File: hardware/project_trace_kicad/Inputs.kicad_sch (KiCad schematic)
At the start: 11 parts, among them J101 Conn_Coaxial, J102 Conn_Coaxial, U101 AD8421, U102 AQW280SX, U103 AQW280SX, U201 ADA4807-1

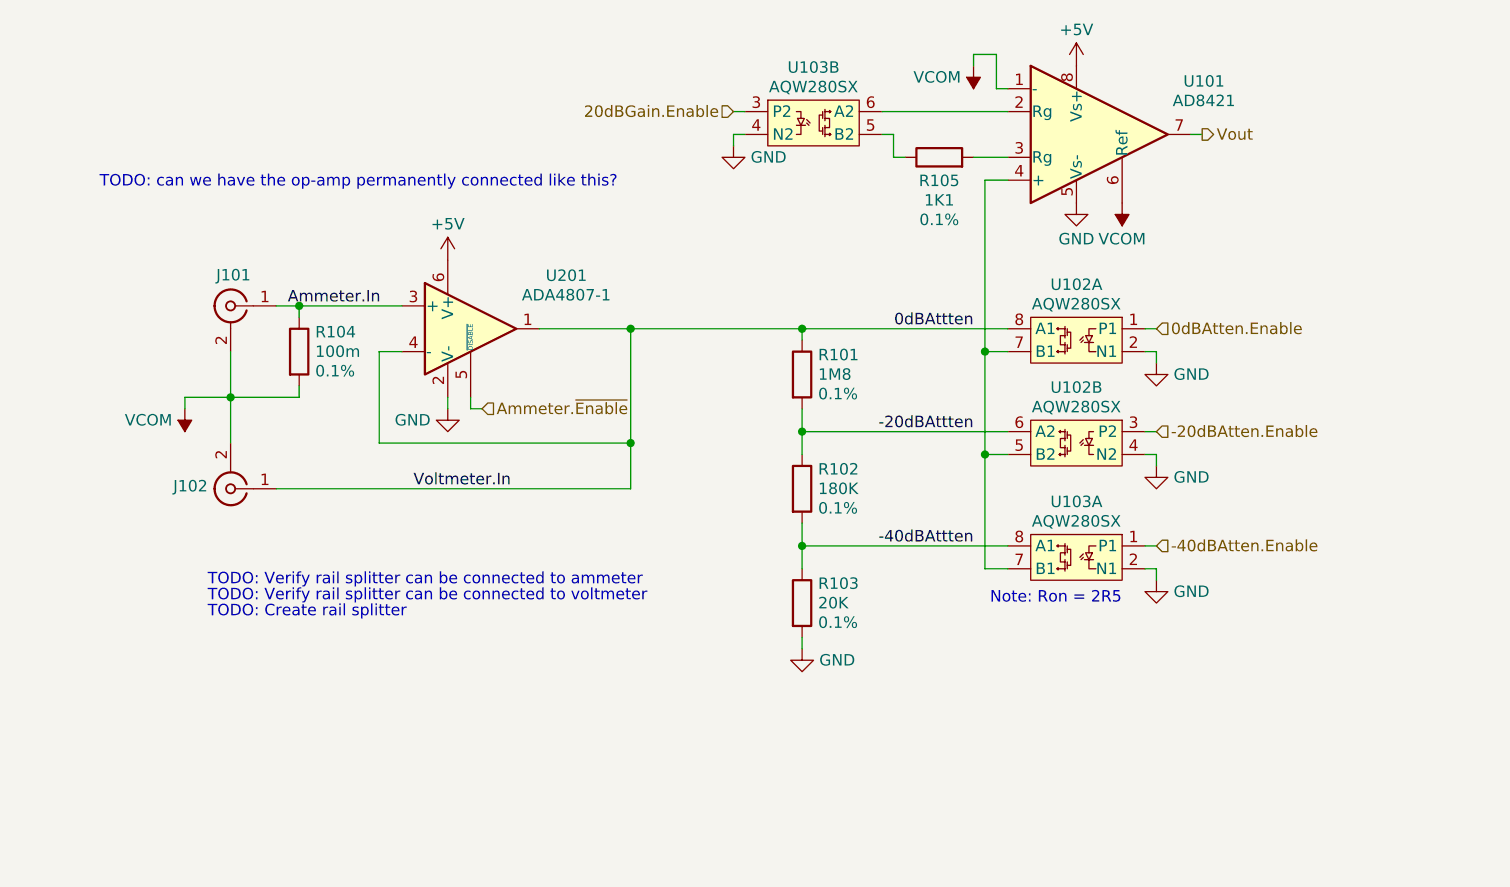
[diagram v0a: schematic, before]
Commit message: Add TVS, Fixes to Ammeter
Fix Ammeter OV Vulnerability
Choose Ammeter Current-Sensing Resistor
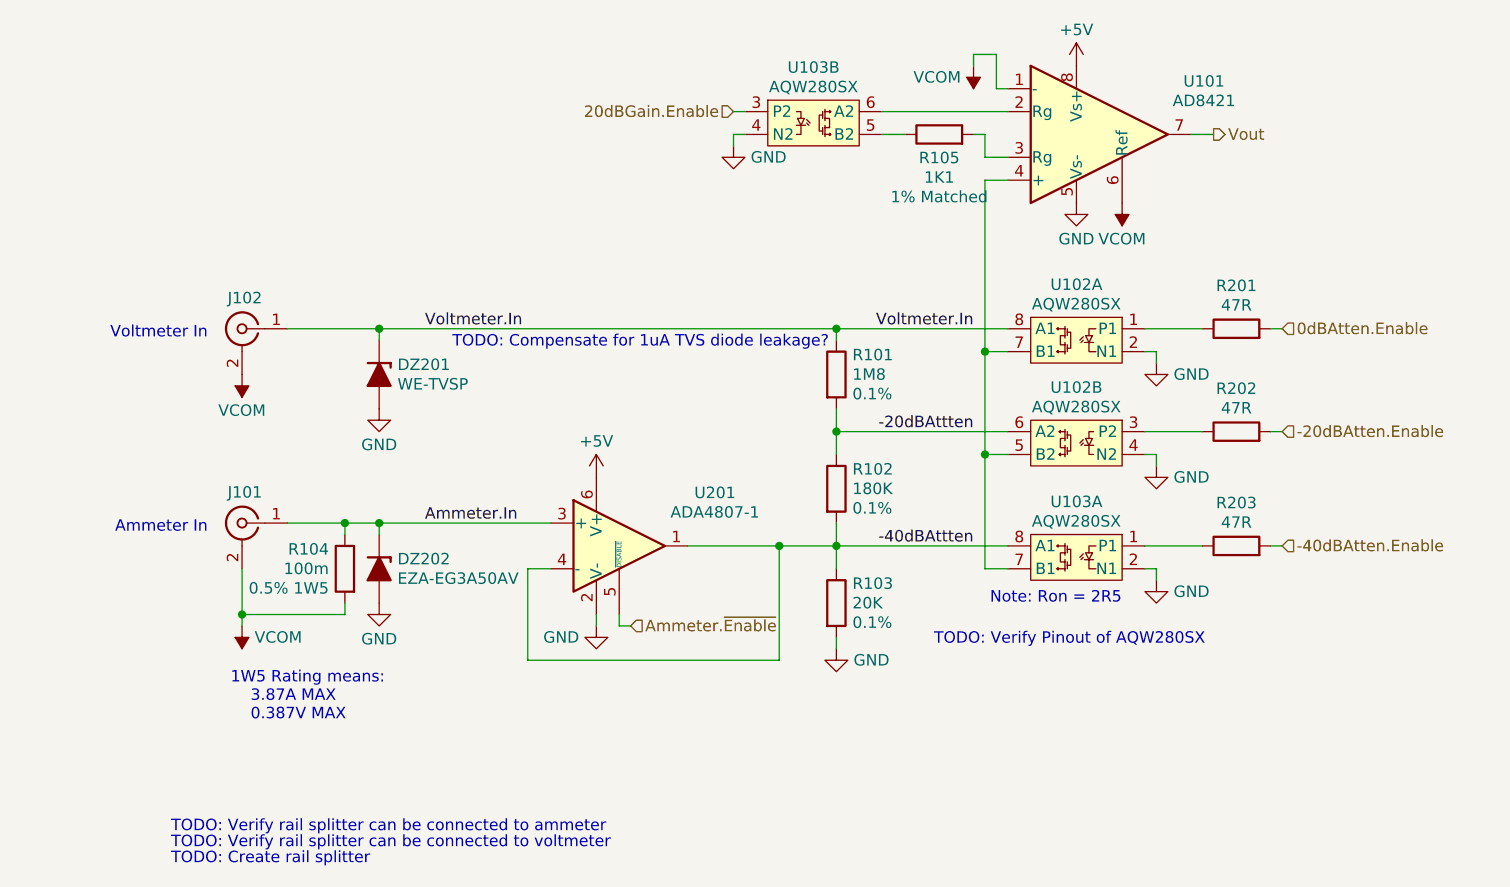
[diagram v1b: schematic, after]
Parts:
- added DZ201: WE-TVSP, Diode_SMD:D_SMC_Handsoldering, symbol PCM_Diode_Zener_AKL:D_Zener_Generic
- added DZ202: EZA-EG3A50AV, Diode_SMD:D_0603_1608Metric_Pad1.05x0.95mm_HandSolder, symbol PCM_Diode_Zener_AKL:D_Zener_Generic
- added R201, R202, R203: 47R, Resistor_SMD:R_0603_1608Metric_Pad0.98x0.95mm_HandSolder, symbol Device:R
- R104: footprint Resistor_SMD:R_0603_1608Metric_Pad0.98x0.95mm_HandSolder -> Resistor_SMD:R_2512_6332Metric_Pad1.40x3.35mm_HandSolder; Extra 0.1% -> 0.5% 1W5; MouserPN (none) -> SLW1TTER100D
- R105: Extra 0.1% -> 1% Matched
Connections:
- net -20dBAtten.Enable: now also R202.2; no longer U102.3 (P2)
- net -40dBAtten.Enable: now also R203.2; no longer U103.1 (P1)
- net -40dBAttten: now also U201.1, U201.4 (-)
- net 0dBAtten.Enable: now also R201.2; no longer U102.1 (P1)
- net Ammeter.In: now also DZ202.1 (K)
- net GND: now also DZ201.2 (A), DZ202.2 (A)
- net 0dBAttten renamed Voltmeter.In
- net Voltmeter.In: now also DZ201.1 (K); no longer U201.1, U201.4 (-)
- new net: R203.1, U103.1 (P1)
- new net: R201.1, U102.1 (P1)
- new net: R202.1, U102.3 (P2)
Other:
- note added: "1W5 Rating means: 3.87A MAX 0.387V MAX"
- note added: "Ammeter In"
- note added: "TODO: Compensate for 1uA TVS diode leakage?"
- note added: "TODO: Verify Pinout of AQW280SX"
- note added: "Voltmeter In"
- note removed: "TODO: can we have the op-amp permanently connected like this?"
- moved on the sheet: J101, J102, R101, R102, R103, R104, R105, U201

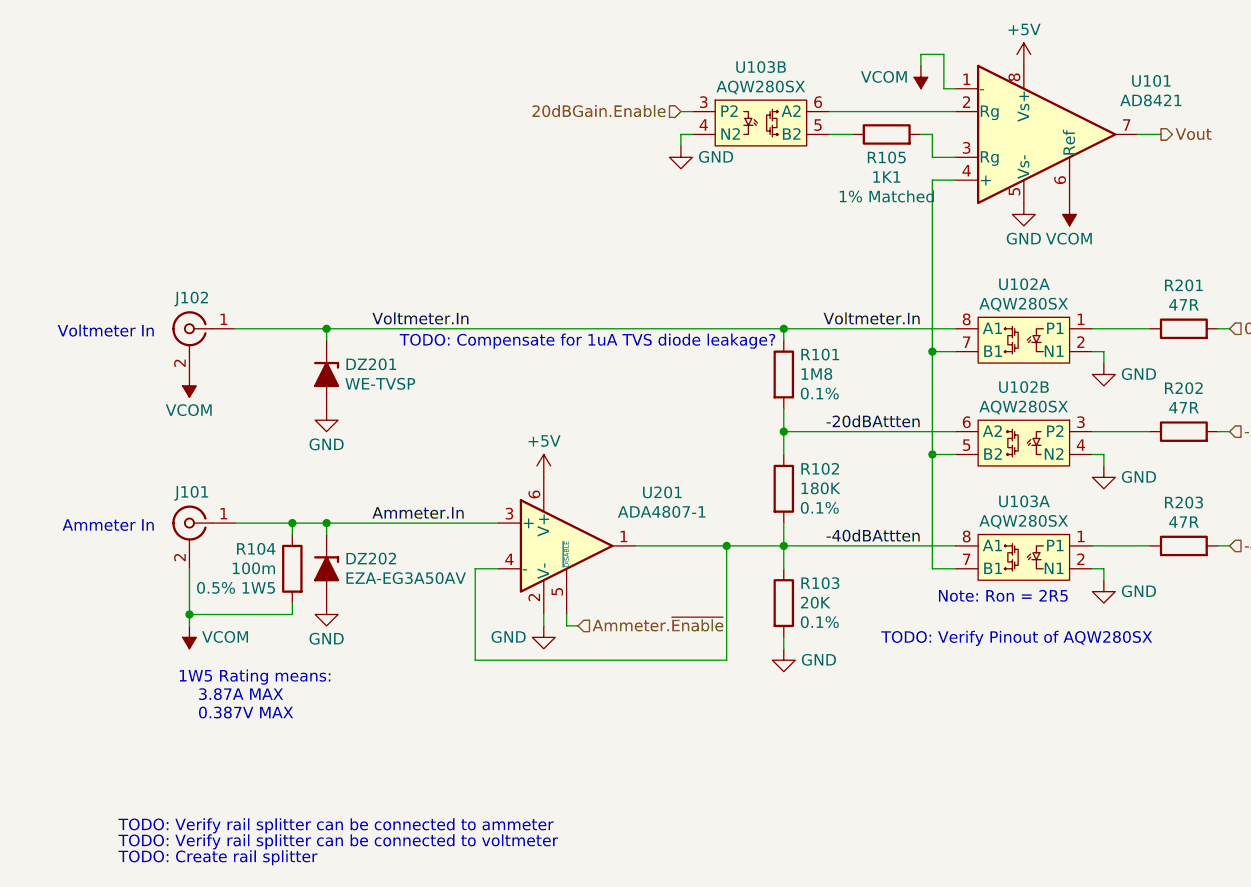
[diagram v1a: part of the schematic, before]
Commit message: Add TVS Diode to VCOM
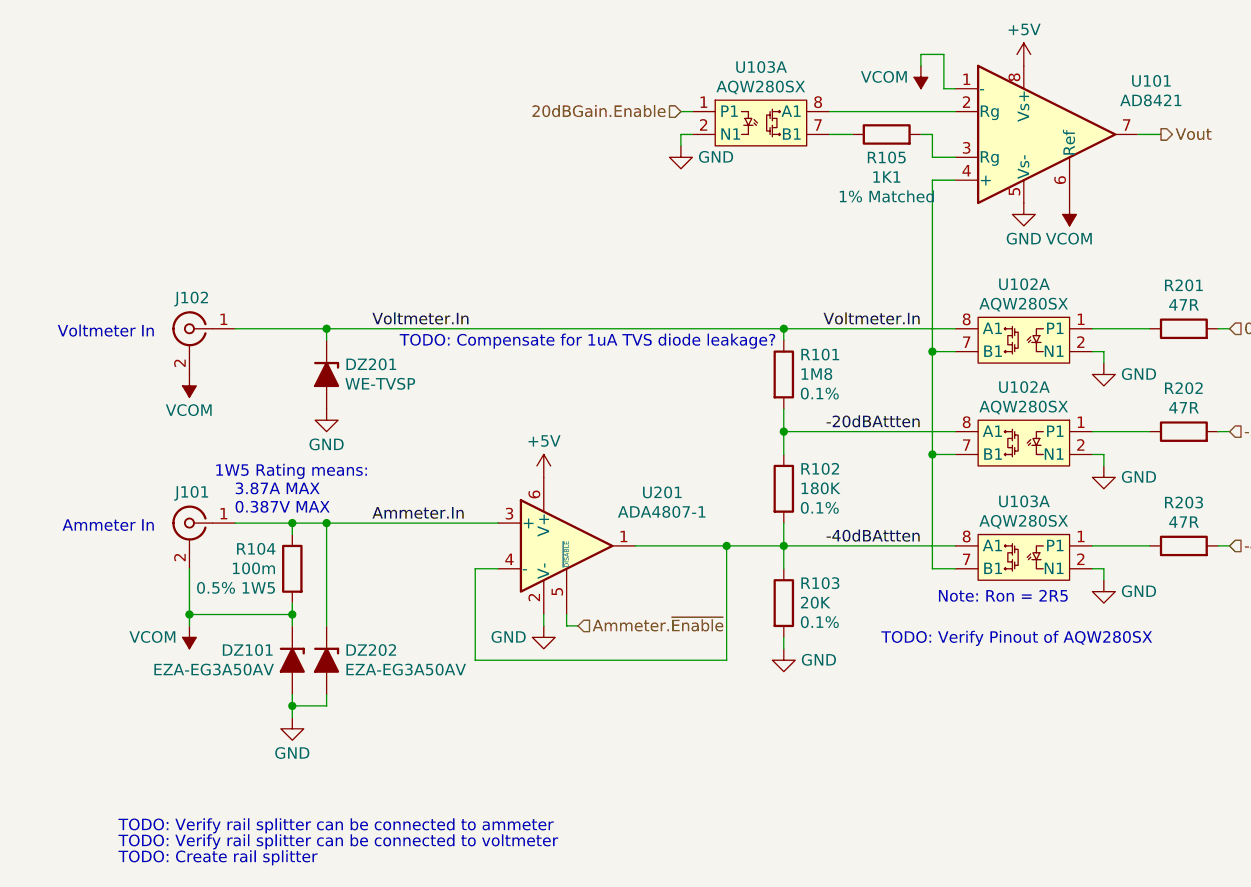
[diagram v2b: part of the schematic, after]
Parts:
- added DZ101: EZA-EG3A50AV, Diode_SMD:D_0603_1608Metric_Pad1.05x0.95mm_HandSolder, symbol PCM_Diode_Zener_AKL:D_Zener_Generic
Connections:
- net -20dBAttten: now also U102.8 (A1); no longer U102.6 (A2)
- net 20dBGain.Enable: now also U103.1 (P1); no longer U103.3 (P2)
- net GND: now also U102.2 (N1), U103.2 (N1), DZ101.2 (A); no longer U102.4 (N2), U103.4 (N2)
- net VCOM: now also DZ101.1 (K)
- net at R105.1: now also U103.7 (B1); no longer U103.5 (B2)
- net at U101.4 (+), U102.7 (B1), U103.7 (B1): now also U102.7 (B1); no longer U102.5 (B2)
- net at R202.1: now also U102.1 (P1); no longer U102.3 (P2)
- net at U101.2 (Rg): now also U103.8 (A1); no longer U103.6 (A2)
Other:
- moved on the sheet: DZ202

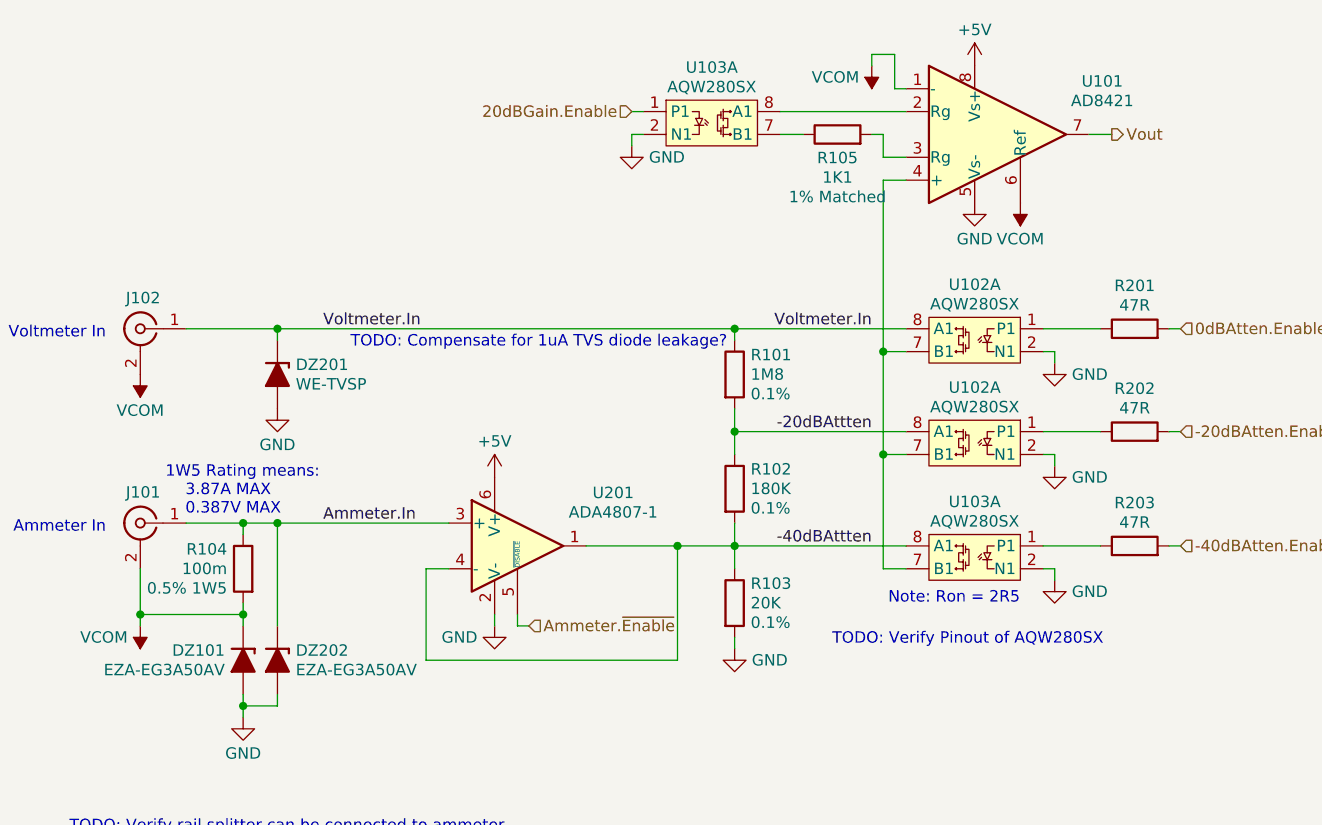
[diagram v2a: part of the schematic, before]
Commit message: Introduce basic design rules, tweak inputs
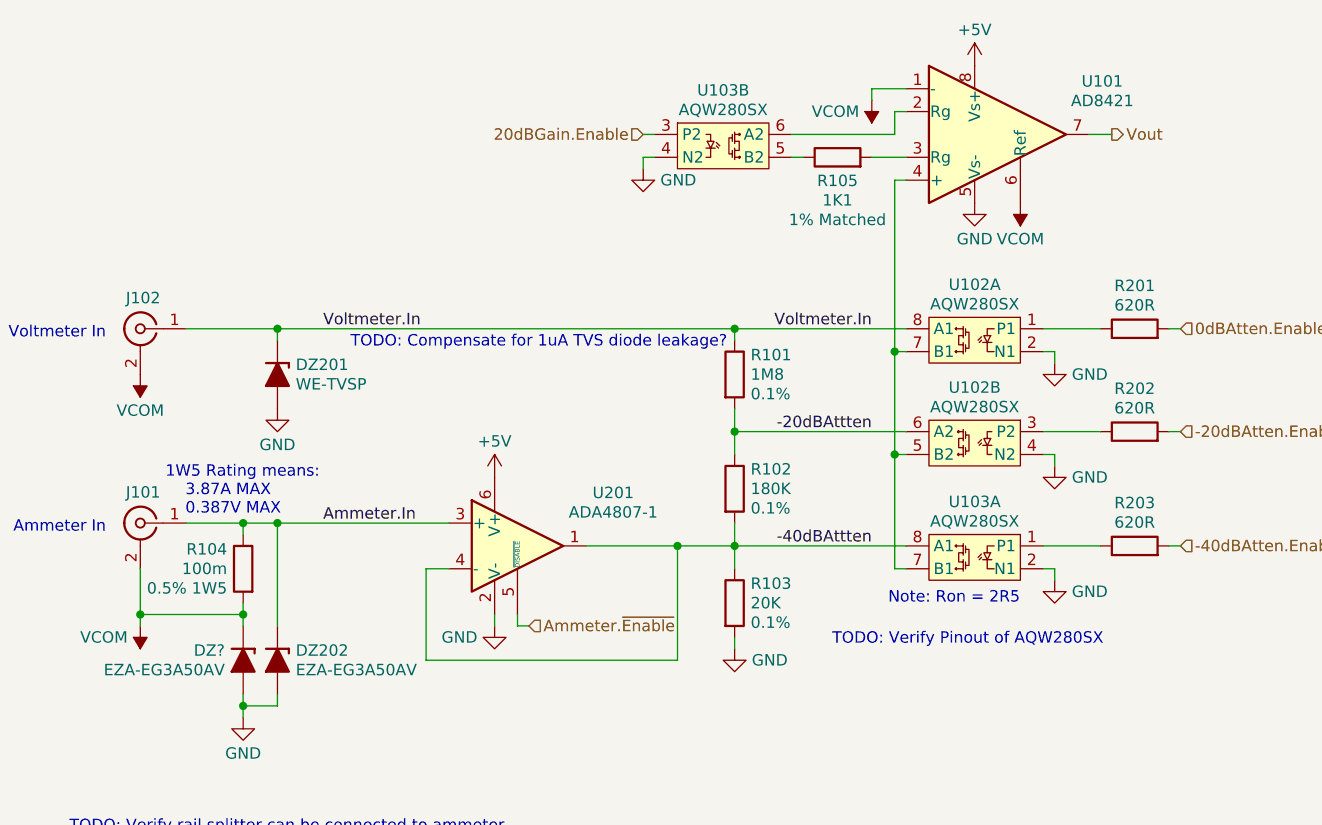
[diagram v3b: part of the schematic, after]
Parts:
- R201, R202, R203: value 47R -> 620R
- renumbered DZ101 to DZ?
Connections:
- net -20dBAttten: now also U102.6 (A2); no longer U102.8 (A1)
- net 20dBGain.Enable: now also U103.3 (P2); no longer U103.1 (P1)
- net GND: now also U102.4 (N2), U103.4 (N2); no longer U102.2 (N1), U103.2 (N1)
- net at R105.1: now also U103.5 (B2); no longer U103.7 (B1)
- net at U101.4 (+), U102.7 (B1), U103.7 (B1): now also U102.5 (B2); no longer U102.7 (B1)
- net at R202.1: now also U102.3 (P2); no longer U102.1 (P1)
- net at U101.2 (Rg): now also U103.6 (A2); no longer U103.8 (A1)
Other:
- moved on the sheet: R105, U103B

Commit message: Rushed Push Footprint Lib
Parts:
- added C201, C202: 1u, symbol Device:C
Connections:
- net +5V: now also C201.1, C202.2
- net GND: now also C201.2, C202.1
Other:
- note added: "TODO: Add Decoupling to Amps"
- note added: "TODO: Use Diff-amp?"
